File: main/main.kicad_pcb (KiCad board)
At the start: 2 copper layers, 45.1 x 52.6 mm, 62 parts, among them P2 CONN_5, P7 CONN_10, P8 CONN_7, U1 MKL03Z32VFK4, U2 IS31FL3737, U4 ESD

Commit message: Assign the same value to microswitches so that they'll be featured in a single BOM line.
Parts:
- SW_MLK1: value MLK -> CMI126603D08
- SW_MRK1: value MRK -> CMI126603D08
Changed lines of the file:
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@@
     (34 B.Paste user)
     (35 F.Paste user)
-    (36 B.SilkS user)
+    (36 B.SilkS user hide)
     (37 F.SilkS user)
     (38 B.Mask user)
@@
       (effects (font (size 0.75 0.75) (thickness 0.15)))
     )
-    (fp_text value MRK (at 0 3.9 150) (layer F.Fab) hide
+    (fp_text value CMI126603D08 (at 0 3.9 150) (layer F.Fab) hide
       (effects (font (size 0.75 0.75) (thickness 0.15)))
     )
@@
       (effects (font (size 0.75 0.75) (thickness 0.15)))
     )
-    (fp_text value MLK (at 0 3.9) (layer F.Fab) hide
-      (effects (font (size 0.75 0.75) (thickness 0.15)))
-    )
+    (fp_text value CMI126603D08 (at 0 3.9) (layer F.Fab) hide
+      (effects (font (size 0.75 0.75) (thickness 0.15)))
+    )

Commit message: Assign the same value to RGB LEDs.
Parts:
- D_TK1: value ugl:RGB_LED -> RGB_LED
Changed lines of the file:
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@@
     (34 B.Paste user)
     (35 F.Paste user)
-    (36 B.SilkS user hide)
+    (36 B.SilkS user)
     (37 F.SilkS user)
     (38 B.Mask user)
@@
       (effects (font (size 0.75 0.75) (thickness 0.15)) (justify mirror))
     )
-    (fp_text value ugl:RGB_LED (at 0 5) (layer B.SilkS) hide
-      (effects (font (size 0.75 0.75) (thickness 0.15)) (justify mirror))
-    )
+    (fp_text value RGB_LED (at 0 5) (layer B.SilkS) hide
+      (effects (font (size 0.75 0.75) (thickness 0.15)) (justify mirror))
+    )

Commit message: Assign the same value to S01 sockets.
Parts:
- SW_LK1: value LK -> S01_Socket
- SW_RK1: value RK -> S01_Socket
- SW_TK1: value TK -> S01_Socket
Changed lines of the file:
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@@
       (effects (font (size 0.75 0.75) (thickness 0.15)) (justify mirror))
     )
-    (fp_text value RK (at 5.2 6.3 150) (layer B.SilkS) hide
+    (fp_text value S01_Socket (at 5.2 6.3 150) (layer B.SilkS) hide
       (effects (font (size 0.75 0.75) (thickness 0.15)) (justify mirror))
     )
@@
       (effects (font (size 0.75 0.75) (thickness 0.15)) (justify mirror))
     )
-    (fp_text value LK (at 5.2 6.3 180) (layer B.SilkS) hide
+    (fp_text value S01_Socket (at 5.2 6.3 180) (layer B.SilkS) hide
       (effects (font (size 0.75 0.75) (thickness 0.15)) (justify mirror))
     )
@@
       (effects (font (size 0.75 0.75) (thickness 0.15)) (justify mirror))
     )
-    (fp_text value TK (at 5.2 6.3 180) (layer B.SilkS) hide
+    (fp_text value S01_Socket (at 5.2 6.3 180) (layer B.SilkS) hide
       (effects (font (size 0.75 0.75) (thickness 0.15)) (justify mirror))
     )

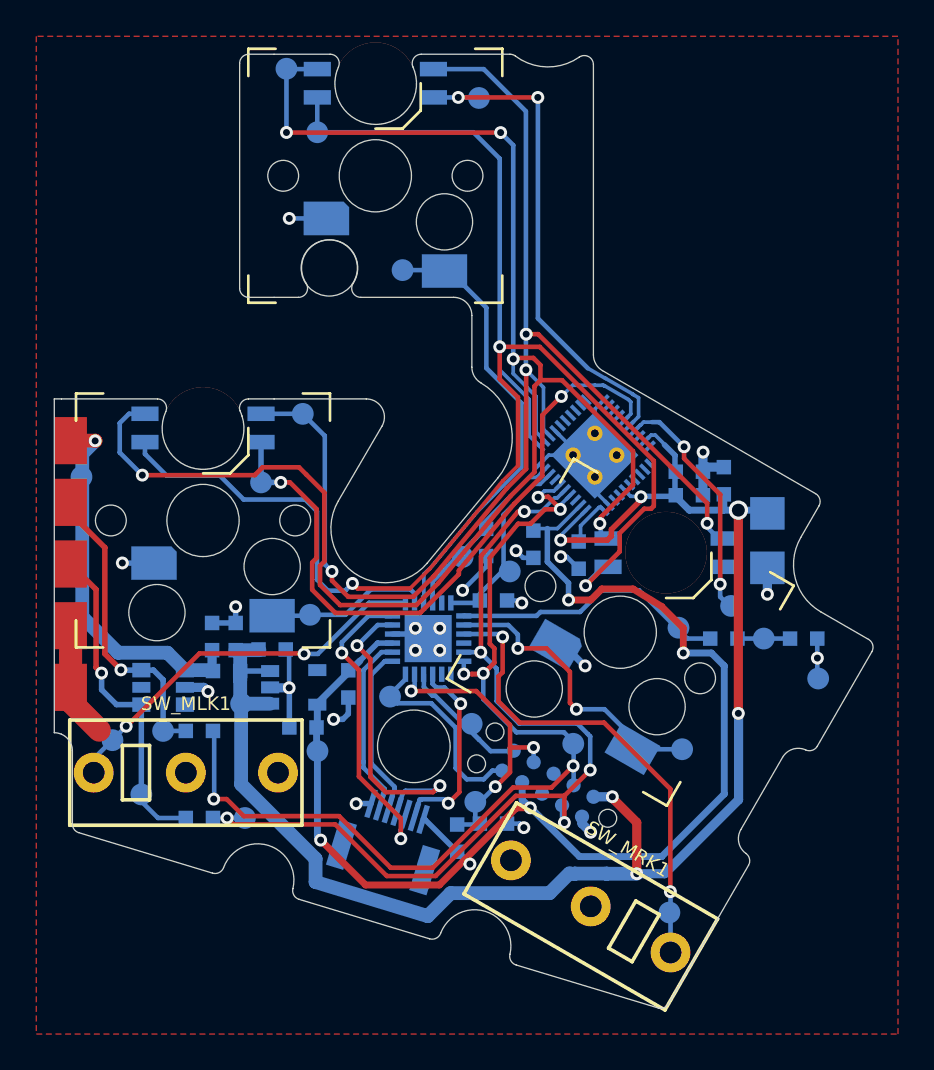
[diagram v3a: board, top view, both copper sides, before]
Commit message: Feature RGB LEDs on the correct side.
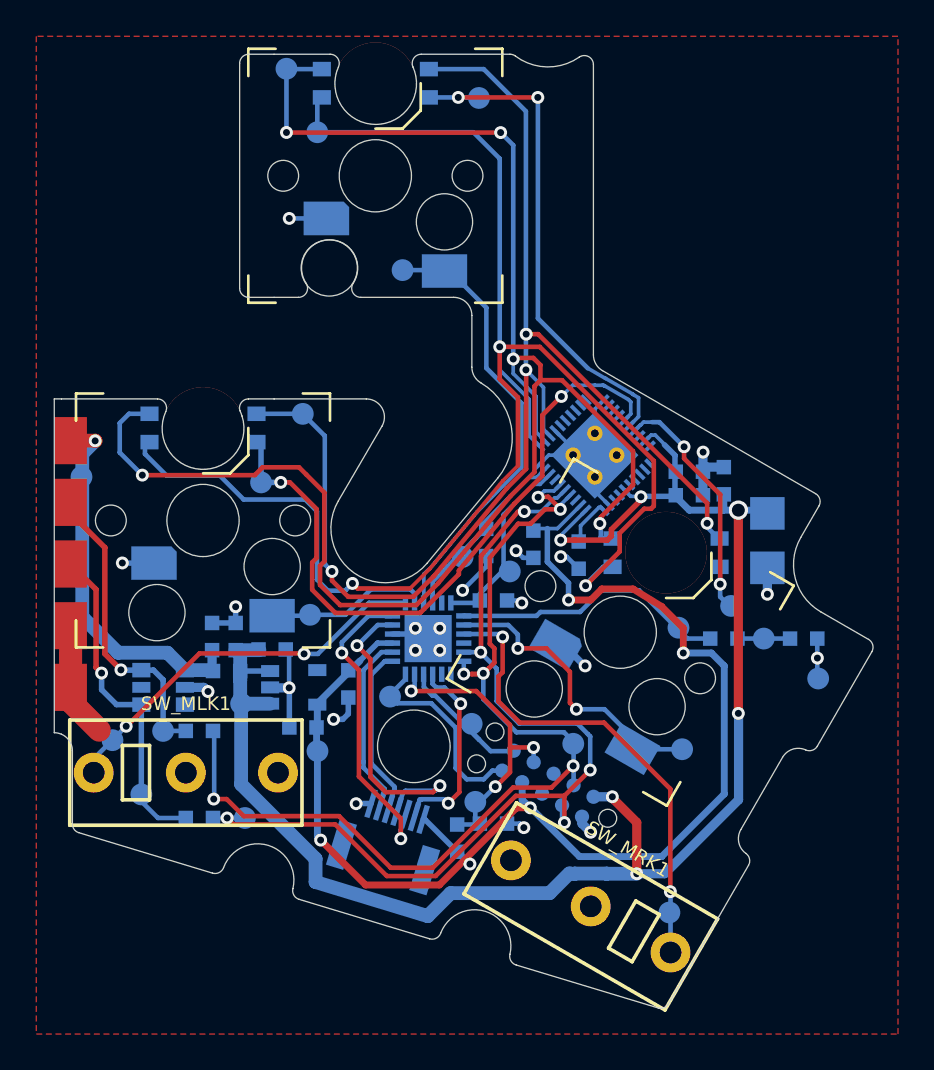
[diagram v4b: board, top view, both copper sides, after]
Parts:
- D_LK1, D_RK1, D_TK1: moved to B.Cu

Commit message: Update sockets and put them on the back side.
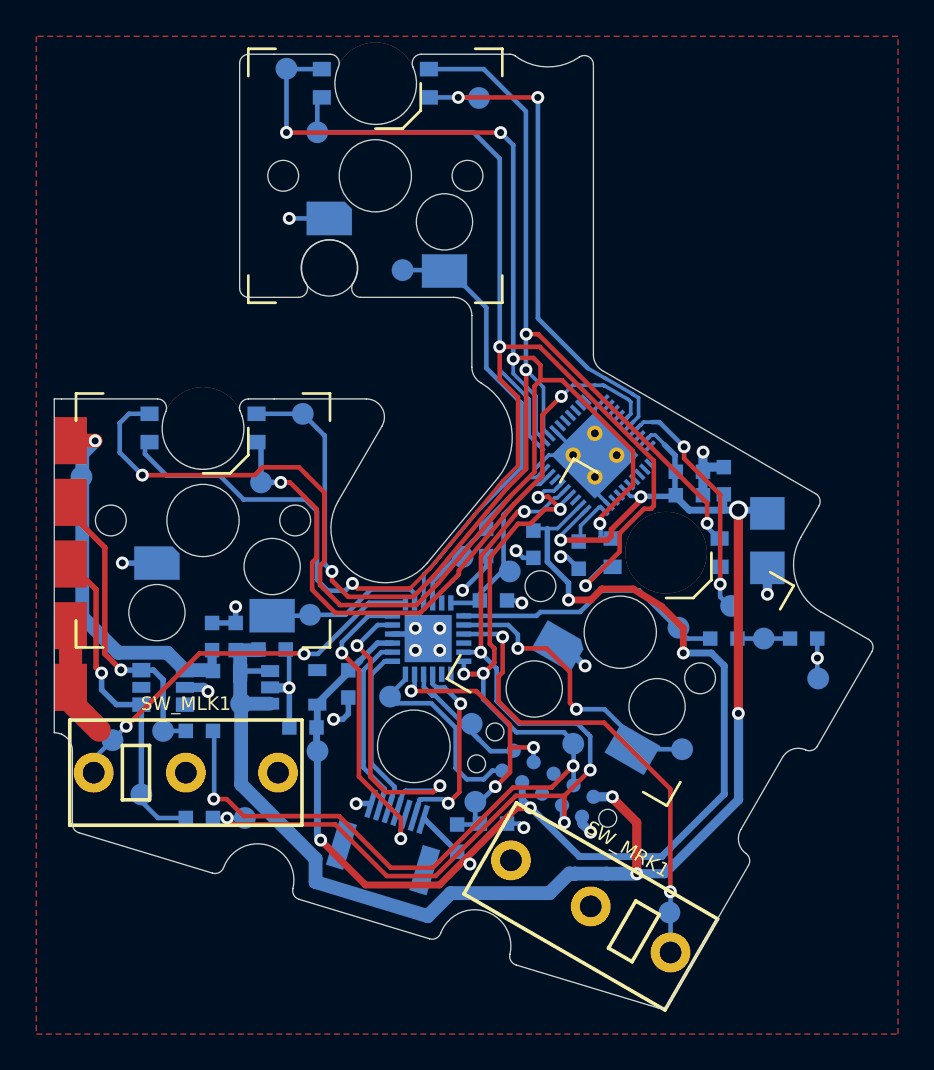
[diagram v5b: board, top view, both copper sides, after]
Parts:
- SW_LK1, SW_RK1, SW_TK1: moved to B.Cu
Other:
- board text added: "51281-0794"

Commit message: Delete test points.
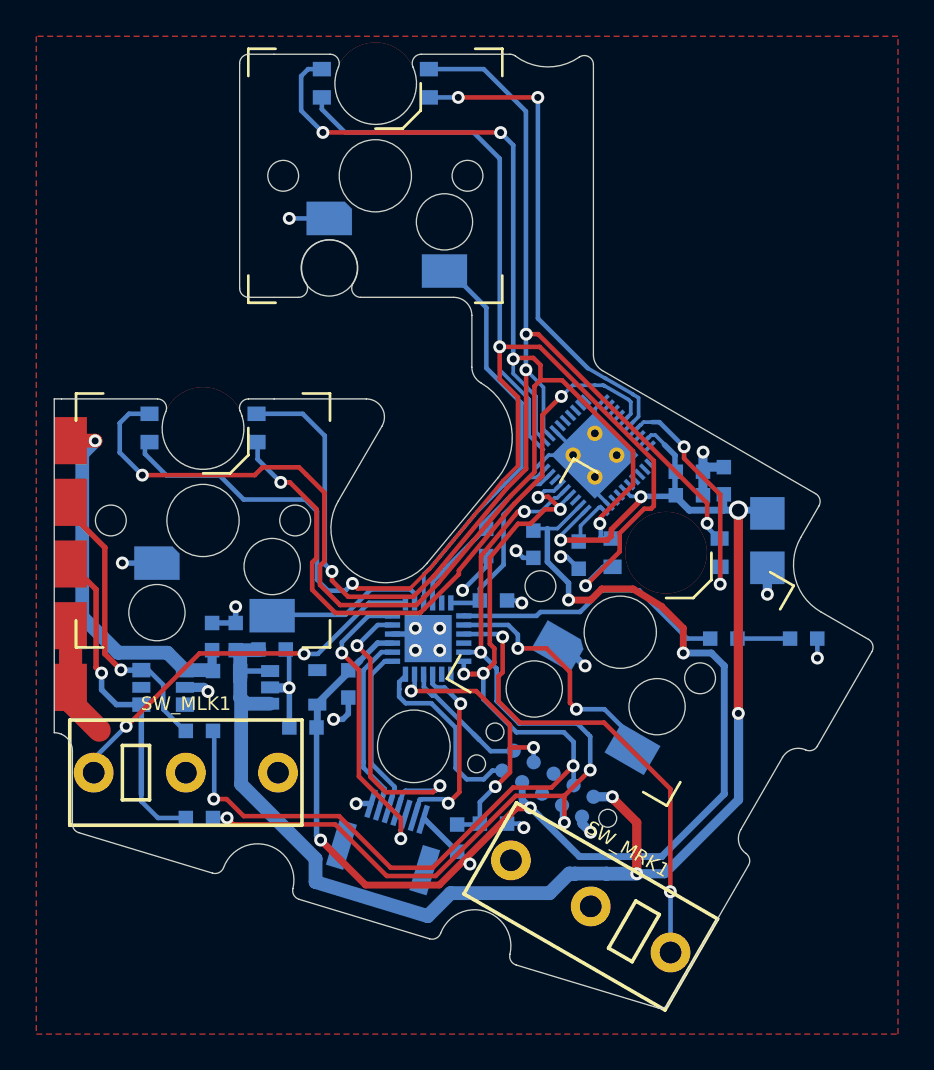
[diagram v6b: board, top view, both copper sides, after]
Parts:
- removed TP_3.3V1: 3.3V, UGL:Test_Point
- removed TP_5V1: 5V, UGL:Test_Point
- removed TP_CS1: LCS1, UGL:Test_Point
- removed TP_CS2: LCS2, UGL:Test_Point
- removed TP_CS3: LCS3, UGL:Test_Point
- removed TP_GND1: GND, UGL:Test_Point
- removed TP_IICRST1: IRST, UGL:Test_Point
- removed TP_KEY_LEFT1: KL, UGL:Test_Point
- removed TP_KEY_MLEFT1: KML, UGL:Test_Point
- removed TP_KEY_MRIGHT1: KMR, UGL:Test_Point
- removed TP_KEY_RIGHT1: KR, UGL:Test_Point
- removed TP_KEY_TOP1: KT, UGL:Test_Point
- removed TP_RESET1: RST, UGL:Test_Point
- removed TP_SCL1: SCL, UGL:Test_Point
- removed TP_SCL_BOTTOM1: SCL_B, UGL:Test_Point
- removed TP_SDA1: SDA, UGL:Test_Point
- removed TP_SDA_BOTTOM1: SDA_B, UGL:Test_Point
- removed TP_SDB1: SDB, UGL:Test_Point
- removed TP_SW1: LSW1, UGL:Test_Point
- removed TP_SW2: LSW2, UGL:Test_Point
- removed TP_SW3: LSW3, UGL:Test_Point
- removed TP_SWDCLK1: SWDCLK, UGL:Test_Point
- removed TP_SWDIO1: SWDIO, UGL:Test_Point
- removed TP_TEST_LED1: TL, UGL:Test_Point
- removed TP_TEST_LED_R1: TLR, UGL:Test_Point
- removed TP_VCC_BOTTOM1: VCC_B, UGL:Test_Point
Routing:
- net /KEY_RIGHT: track 16.8 -> 14.1 mm
- net /LED_SW2: track 91.9 -> 89.5 mm
- net /KEY_TOP: track 24.7 -> 22.4 mm
- net /SCL: track 52.5 -> 50.5 mm
- net /LED_CS3: track 14.4 -> 12.9 mm
- net GND: track 47.9 -> 46.9 mm
- net /LED_SW1: track 87.9 -> 86.9 mm
- net /LED_CS2: track 27.9 -> 27.0 mm
- net /SDA_BOTTOM: track 17.0 -> 16.1 mm
- net /LED_CS1: track 37.6 -> 36.9 mm
- net /SWDIO: track 11.5 -> 10.9 mm

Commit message: Improve silk screen.
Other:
- board text removed: "U1 P/N:"
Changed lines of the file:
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@@
   (general
     (thickness 1.6)
-    (drawings 106)
+    (drawings 97)
     (tracks 667)
     (zones 0)
@@
   (module UGL:S01_Hybrid_Socket locked (layer B.Cu)
     (at 133.2 106.7 180)
-    (fp_text reference SW_LK1 (at -6.509512 -0.610302 90) (layer B.SilkS)
+    (fp_text reference SW_LK1 (at -6.209512 -2.710302 90) (layer B.SilkS)
       (effects (font (size 0.75 0.75) (thickness 0.15)) (justify mirror))
     )
@@
   (module UGL:S01_Hybrid_Socket locked (layer B.Cu)
     (at 156.2 112.86 150)
-    (fp_text reference SW_RK1 (at -6.678837 -7.749061 110) (layer B.SilkS)
+    (fp_text reference SW_RK1 (at -6.164478 -3.658164 240) (layer B.SilkS)
       (effects (font (size 0.75 0.75) (thickness 0.15)) (justify mirror))
     )
@@
     (at 158.725 108.475)
     (attr smd)
-    (fp_text reference D_RK1 (at 1.084512 3.035302) (layer B.SilkS)
+    (fp_text reference D_RK1 (at 0.984512 2.835302) (layer B.SilkS)
       (effects (font (size 0.75 0.75) (thickness 0.15)) (justify mirror))
     )
@@
     (at 142.7 82.6)
     (attr smd)
-    (fp_text reference D_TK1 (at 3.109512 2.710302) (layer B.SilkS)
+    (fp_text reference D_TK1 (at -4.290488 0.210302 90) (layer B.SilkS)
       (effects (font (size 0.75 0.75) (thickness 0.15)) (justify mirror))
     )
@@
     (tags "Tag-Connect TC2050")
     (attr virtual)
-    (fp_text reference P7 (at -5.372008 -1.569072 150) (layer B.SilkS)
+    (fp_text reference P7 (at -4.880127 1.547372 150) (layer B.SilkS)
       (effects (font (size 0.75 0.75) (thickness 0.15)) (justify mirror))
     )
@@
     (at 147.209512 124.210302 90)
     (attr smd)
-    (fp_text reference R1 (at -3 -0.9 90) (layer B.SilkS)
-      (effects (font (size 0.75 0.75) (thickness 0.15)) (justify mirror))
-    )
-    (fp_text value 4.7K (at -2.5 0.1 90) (layer B.SilkS)
+    (fp_text reference R1 (at -1.9 -0.3 180) (layer B.SilkS)
+      (effects (font (size 0.75 0.75) (thickness 0.15)) (justify mirror))
+    )
+    (fp_text value 4.7K (at -3 -0.2 180) (layer B.SilkS)
       (effects (font (size 0.75 0.75) (thickness 0.15)) (justify mirror))
     )
@@
     (at 137.009512 113.810302 180)
     (attr smd)
-    (fp_text reference C2 (at -3.7 2.2 180) (layer B.SilkS)
-      (effects (font (size 0.75 0.75) (thickness 0.15)) (justify mirror))
-    )
-    (fp_text value 1uF (at -4 1.1) (layer B.SilkS)
+    (fp_text reference C2 (at -2.2 1.7 180) (layer B.SilkS)
+      (effects (font (size 0.75 0.75) (thickness 0.15)) (justify mirror))
+    )
+    (fp_text value 1uF (at -2.5 0.6) (layer B.SilkS)
       (effects (font (size 0.75 0.75) (thickness 0.15)) (justify mirror))
     )
@@
     (clearance 0.09)
     (attr smd)
-    (fp_text reference U2 (at -4.22863 -3.252133 90) (layer B.SilkS)
+    (fp_text reference U2 (at -4.440762 1.061219 90) (layer B.SilkS)
       (effects (font (size 0.746 0.746) (thickness 0.15)) (justify mirror))
     )
-    (fp_text value IS31FL3737 (at -7.481321 -6.504824 270) (layer B.SilkS)
+    (fp_text value IS31FL3737 (at -5.501422 -1.555076 270) (layer B.SilkS)
       (effects (font (size 0.746 0.746) (thickness 0.15)) (justify mirror))
     )
@@
     (at 138.709512 118.110302)
     (attr smd)
-    (fp_text reference C12 (at 2.5 0 270) (layer B.SilkS)
-      (effects (font (size 0.75 0.75) (thickness 0.15)) (justify mirror))
-    )
-    (fp_text value 1uF (at 2.5 2.5 90) (layer B.SilkS)
+    (fp_text reference C12 (at 0.7 1.3) (layer B.SilkS)
+      (effects (font (size 0.75 0.75) (thickness 0.15)) (justify mirror))
+    )
+    (fp_text value 1uF (at 0.8 2.4 180) (layer B.SilkS)
       (effects (font (size 0.75 0.75) (thickness 0.15)) (justify mirror))
     )
@@
       (effects (font (size 0.75 0.75) (thickness 0.15)) (justify mirror))
     )
-    (fp_text value 47 (at -1.409512 -2.310302 180) (layer B.SilkS)
+    (fp_text value 47 (at -1.209512 -2.310302 180) (layer B.SilkS)
       (effects (font (size 0.75 0.75) (thickness 0.15)) (justify mirror))
     )
@@
     (at 161.909512 113.210302 180)
     (attr smd)
-    (fp_text reference R2 (at -0.2 -1.2 180) (layer B.SilkS)
-      (effects (font (size 0.75 0.75) (thickness 0.15)) (justify mirror))
-    )
-    (fp_text value 330 (at -0.6 -2.3 180) (layer B.SilkS)
+    (fp_text reference R2 (at -0.5 1.2 180) (layer B.SilkS)
+      (effects (font (size 0.75 0.75) (thickness 0.15)) (justify mirror))
+    )
+    (fp_text value 330 (at -0.4 -1.2 180) (layer B.SilkS)
       (effects (font (size 0.75 0.75) (thickness 0.15)) (justify mirror))
     )
@@
       (effects (font (size 0.75 0.75) (thickness 0.15)) (justify mirror))
     )
-    (fp_text value 100K (at 1.9 0.5) (layer B.SilkS)
+    (fp_text value 100K (at 0.3 1.1 90) (layer B.SilkS)
       (effects (font (size 0.75 0.75) (thickness 0.15)) (justify mirror))
     )
@@
     (at 166.309512 113.210302 180)
     (attr smd)
-    (fp_text reference D2 (at 0.5 -1.2 180) (layer B.SilkS)
-      (effects (font (size 0.75 0.75) (thickness 0.15)) (justify mirror))
-    )
-    (fp_text value LED (at 0 -1.3 180) (layer B.SilkS) hide
+    (fp_text reference D2 (at 0 1.1 180) (layer B.SilkS)
+      (effects (font (size 0.75 0.75) (thickness 0.15)) (justify mirror))
+    )
+    (fp_text value LED (at 0.6 -1.2 180) (layer B.SilkS)
       (effects (font (size 0.75 0.75) (thickness 0.15)) (justify mirror))
     )
@@
     (clearance 0.1)
     (attr smd)
-    (fp_text reference U1 (at 2.9 2.4) (layer B.SilkS)
-      (effects (font (size 0.75 0.75) (thickness 0.15)) (justify mirror))
-    )
-    (fp_text value MKL03Z32VFK4 (at 9 18.6 343) (layer B.SilkS)
-      (effects (font (size 0.75 0.75) (thickness 0.15)) (justify mirror))
+    (fp_text reference U1 (at 3 2.5) (layer B.SilkS)
+      (effects (font (size 0.75 0.75) (thickness 0.15)) (justify mirror))
+    )
+    (fp_text value MKL03Z32VFK4 (at 0.1 3.5) (layer B.SilkS)
+      (effects (font (size 0.7 0.7) (thickness 0.14)) (justify mirror))
     )
     (fp_line (start -2.15 1.6) (end -2.15 2.15) (layer B.SilkS) (width 0.15))
@@
     (at 131 115.9 270)
     (attr smd)
-    (fp_text reference U4 (at 0.310302 2.390488 270) (layer B.SilkS)
-      (effects (font (size 0.75 0.75) (thickness 0.15)) (justify mirror))
-    )
-    (fp_text value ESD (at -2.1 0 180) (layer B.Fab) hide
+    (fp_text reference U4 (at 0.110302 2.590488) (layer B.SilkS)
+      (effects (font (size 0.75 0.75) (thickness 0.15)) (justify mirror))
+    )
+    (fp_text value ESD (at 1.210302 2.890488 180) (layer B.SilkS)
       (effects (font (size 0.75 0.75) (thickness 0.15)) (justify mirror))
     )
@@
     (at 134.5 115)
     (attr smd)
-    (fp_text reference FB2 (at -0.290488 1.710302 90) (layer B.SilkS)
+    (fp_text reference FB2 (at 0.309512 1.210302 180) (layer B.SilkS)
       (effects (font (size 0.75 0.75) (thickness 0.15)) (justify mirror))
     )
@@
     (tags SOT23)
     (attr smd)
-    (fp_text reference VR1 (at -1.989698 -1.609512) (layer B.SilkS)
+    (fp_text reference VR1 (at 2.010302 2.190488) (layer B.SilkS)
       (effects (font (size 0.75 0.75) (thickness 0.15)) (justify mirror))
     )
@@
     (at 151.409512 108.010302 270)
     (attr smd)
-    (fp_text reference C19 (at -3.3 0.6 90) (layer B.SilkS)
+    (fp_text reference C19 (at -1 1.1 90) (layer B.SilkS)
       (effects (font (size 0.75 0.75) (thickness 0.15)) (justify mirror))
     )
@@
     (at 141.209512 115.710302 90)
     (attr smd)
-    (fp_text reference C4 (at 4.8 1.3 90) (layer B.SilkS)
-      (effects (font (size 0.75 0.75) (thickness 0.15)) (justify mirror))
-    )
-    (fp_text value 0.1uF (at 2.2 1.3 90) (layer B.SilkS)
+    (fp_text reference C4 (at -2.2 0 270) (layer B.SilkS)
+      (effects (font (size 0.75 0.75) (thickness 0.15)) (justify mirror))
+    )
+    (fp_text value 0.1uF (at -4.8 0 270) (layer B.SilkS)
       (effects (font (size 0.75 0.75) (thickness 0.15)) (justify mirror))
     )
@@
   (gr_line (start 158.809512 102.510302) (end 159.509512 103.210302) (layer B.SilkS) (width 0.15))
   (gr_line (start 158.809512 101.610302) (end 158.809512 102.510302) (layer B.SilkS) (width 0.15))
-  (gr_line (start 142.209512 117.210302) (end 142.709512 116.710302) (layer B.SilkS) (width 0.15))
-  (gr_line (start 142.209512 117.410302) (end 142.209512 117.210302) (layer B.SilkS) (width 0.15))
-  (gr_text "U1 P/N:" (at 154.709512 130.510302 343) (layer B.SilkS)
-    (effects (font (size 0.75 0.75) (thickness 0.15)) (justify mirror))
-  )
-  (gr_line (start 146.409512 108.810302) (end 146.709512 108.810302) (layer B.SilkS) (width 0.15))
-  (gr_line (start 145.709512 109.510302) (end 146.409512 108.810302) (layer B.SilkS) (width 0.15))
-  (gr_line (start 151.509512 106.010302) (end 151.509512 106.610302) (layer B.SilkS) (width 0.15))
-  (gr_line (start 151.309512 105.810302) (end 151.509512 106.010302) (layer B.SilkS) (width 0.15))
-  (gr_line (start 139.009512 112.710302) (end 138.309512 113.410302) (layer B.SilkS) (width 0.15))
-  (gr_line (start 139.909512 112.710302) (end 139.009512 112.710302) (layer B.SilkS) (width 0.15))
   (gr_text "PCB ID:\nkeycluster_main_1.0.0" (at 162.493312 121.437542 60) (layer B.SilkS)
     (effects (font (size 0.75 0.75) (thickness 0.15)) (justify mirror))
